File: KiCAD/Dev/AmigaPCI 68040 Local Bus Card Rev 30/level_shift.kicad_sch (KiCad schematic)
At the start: 26 parts, among them U101 74LVC245, U102 74LVC245, U103 74LVC245, U104 74LVC245, U105 74LVC245, U106 74LVC245, U107 74LVC245, U108 74LVC245, U109 SN74LVC16T245DLR, U110 SN74LVC16T245DLR

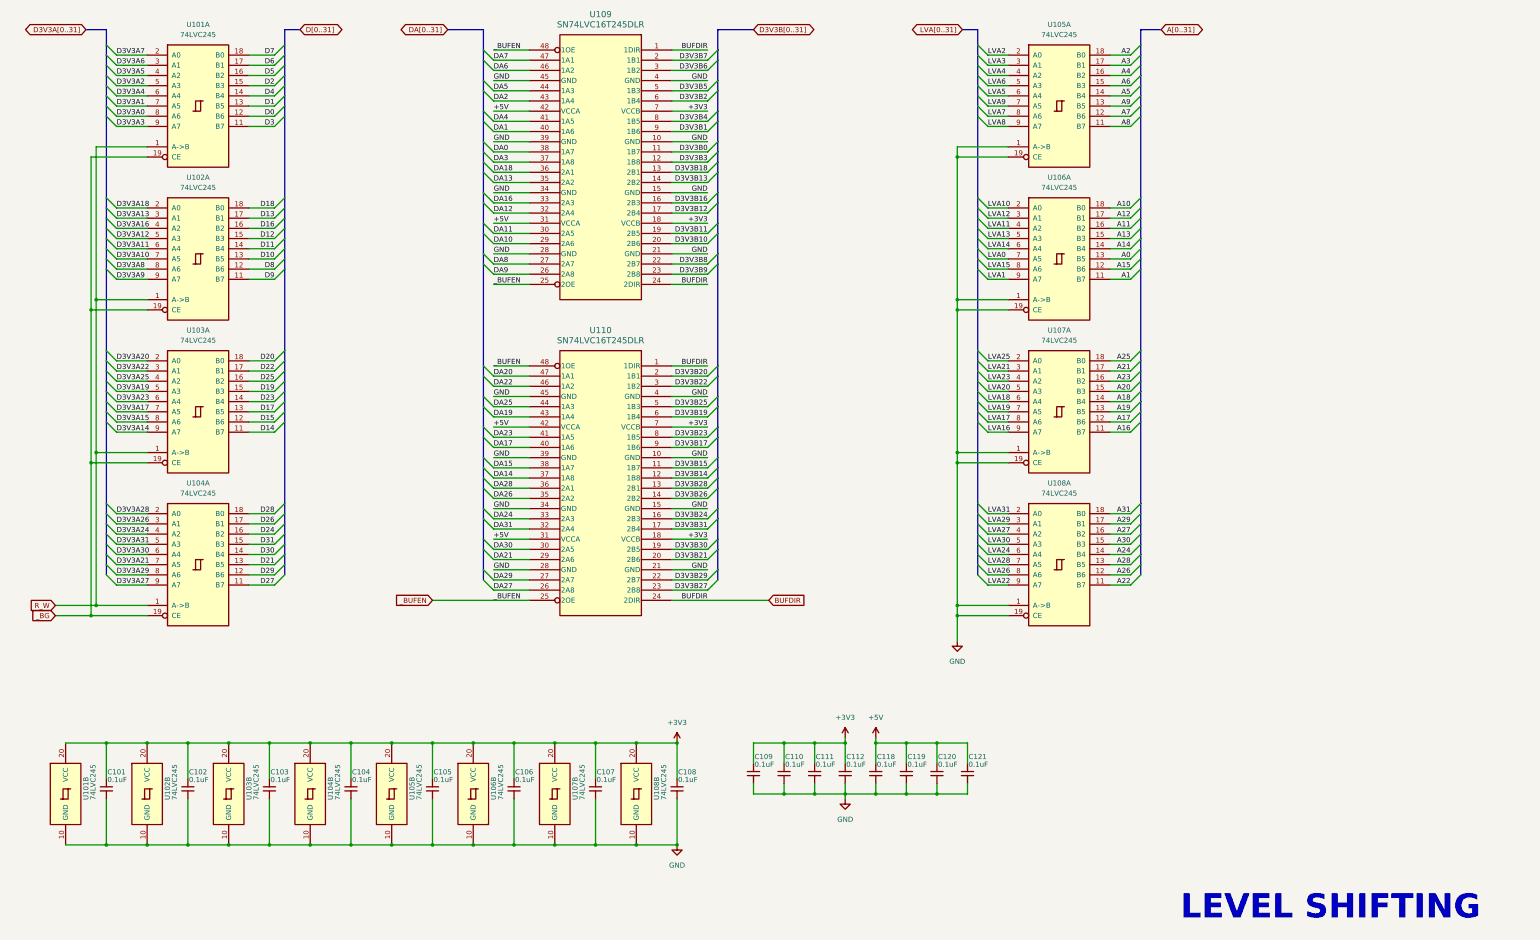
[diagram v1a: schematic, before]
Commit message: PCB Routing CPU Card 10-JUL-2024
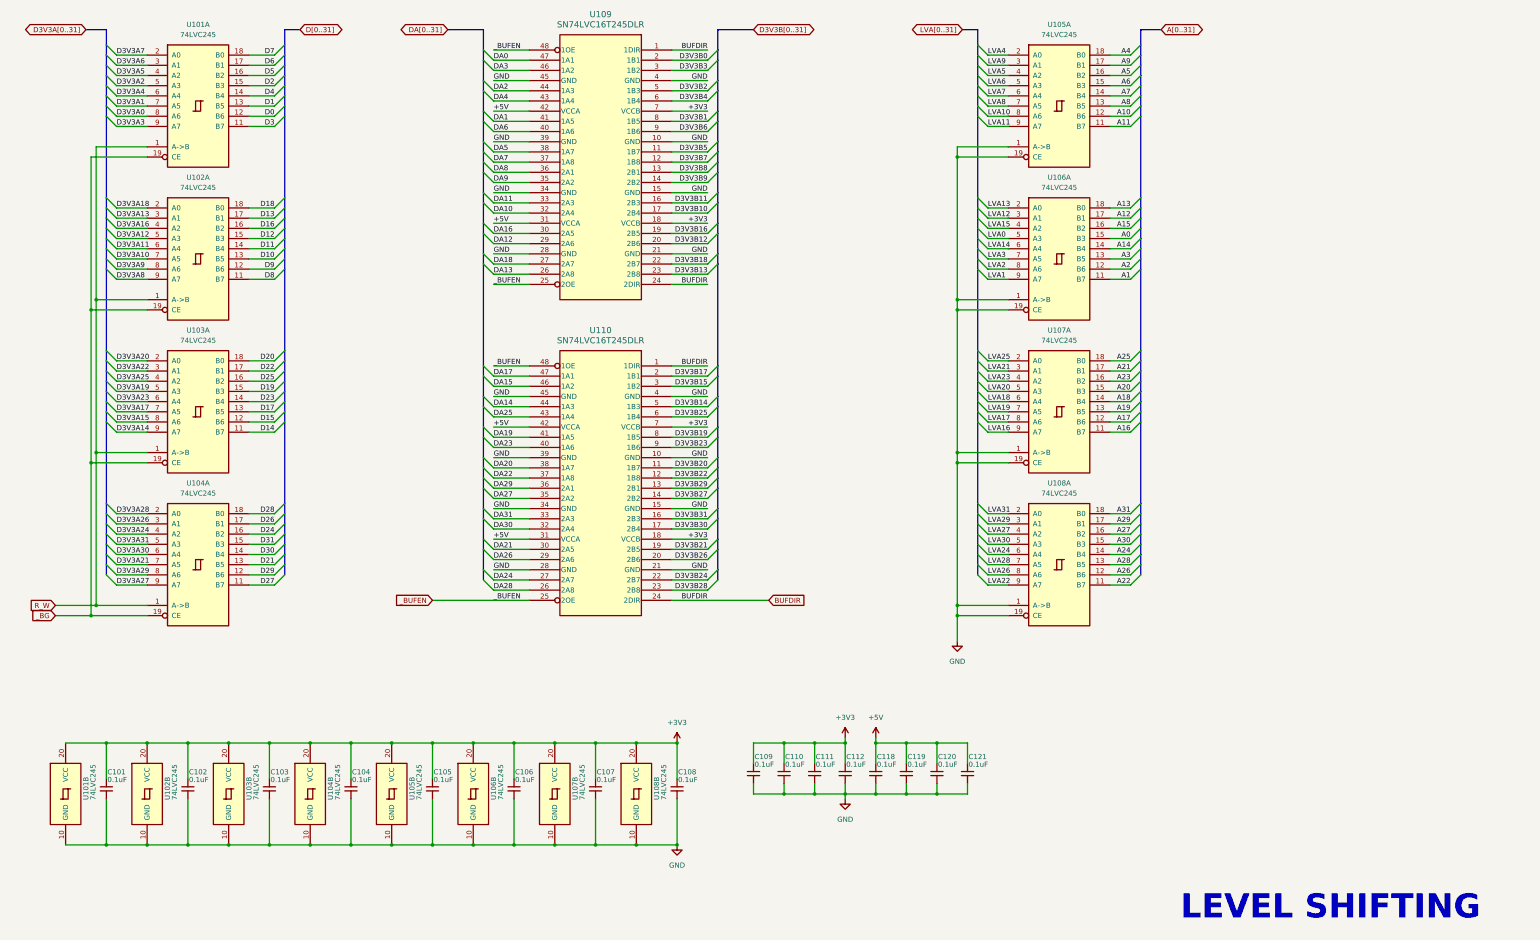
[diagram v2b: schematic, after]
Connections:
- net A0: now also U106.15 (B3); no longer U106.13 (B5)
- net A10: now also U105.12 (B6); no longer U106.18 (B0)
- net A11: now also U105.11 (B7); no longer U106.16 (B2)
- net A13: now also U106.18 (B0); no longer U106.15 (B3)
- net A15: now also U106.16 (B2); no longer U106.12 (B6)
- net A2: now also U106.12 (B6); no longer U105.18 (B0)
- net A3: now also U106.13 (B5); no longer U105.17 (B1)
- net A4: now also U105.18 (B0); no longer U105.16 (B2)
- net A5: now also U105.16 (B2); no longer U105.14 (B4)
- net A7: now also U105.14 (B4); no longer U105.12 (B6)
- net A8: now also U105.13 (B5); no longer U105.11 (B7)
- net A9: now also U105.17 (B1); no longer U105.13 (B5)
- net D3V3A8: now also U102.9 (A7); no longer U102.8 (A6)
- net D3V3A9: now also U102.8 (A6); no longer U102.9 (A7)
- net D3V3B0: now also U109.2 (1B1); no longer U109.11 (1B7)
- net D3V3B1: now also U109.8 (1B5); no longer U109.9 (1B6)
- net D3V3B10: now also U109.17 (2B4); no longer U109.20 (2B6)
- net D3V3B11: now also U109.16 (2B3); no longer U109.19 (2B5)
- net D3V3B12: now also U109.20 (2B6); no longer U109.17 (2B4)
- net D3V3B13: now also U109.23 (2B8); no longer U109.14 (2B2)
- net D3V3B14: now also U110.5 (1B3); no longer U110.12 (1B8)
- net D3V3B15: now also U110.3 (1B2); no longer U110.11 (1B7)
- net D3V3B16: now also U109.19 (2B5); no longer U109.16 (2B3)
- net D3V3B17: now also U110.2 (1B1); no longer U110.9 (1B6)
- net D3V3B18: now also U109.22 (2B7); no longer U109.13 (2B1)
- net D3V3B19: now also U110.8 (1B5); no longer U110.6 (1B4)
- net D3V3B2: now also U109.5 (1B3); no longer U109.6 (1B4)
- net D3V3B20: now also U110.11 (1B7); no longer U110.2 (1B1)
- net D3V3B21: now also U110.19 (2B5); no longer U110.20 (2B6)
- net D3V3B22: now also U110.12 (1B8); no longer U110.3 (1B2)
- net D3V3B23: now also U110.9 (1B6); no longer U110.8 (1B5)
- net D3V3B24: now also U110.22 (2B7); no longer U110.16 (2B3)
- net D3V3B25: now also U110.6 (1B4); no longer U110.5 (1B3)
- net D3V3B26: now also U110.20 (2B6); no longer U110.14 (2B2)
- net D3V3B27: now also U110.14 (2B2); no longer U110.23 (2B8)
- net D3V3B28: now also U110.23 (2B8); no longer U110.13 (2B1)
- net D3V3B29: now also U110.13 (2B1); no longer U110.22 (2B7)
- net D3V3B3: now also U109.3 (1B2); no longer U109.12 (1B8)
- net D3V3B30: now also U110.17 (2B4); no longer U110.19 (2B5)
- net D3V3B31: now also U110.16 (2B3); no longer U110.17 (2B4)
- net D3V3B4: now also U109.6 (1B4); no longer U109.8 (1B5)
- net D3V3B5: now also U109.11 (1B7); no longer U109.5 (1B3)
- net D3V3B6: now also U109.9 (1B6); no longer U109.3 (1B2)
- net D3V3B7: now also U109.12 (1B8); no longer U109.2 (1B1)
- net D3V3B8: now also U109.13 (2B1); no longer U109.22 (2B7)
- net D3V3B9: now also U109.14 (2B2); no longer U109.23 (2B8)
- net D8: now also U102.11 (B7); no longer U102.12 (B6)
- net D9: now also U102.12 (B6); no longer U102.11 (B7)
- net DA0: now also U109.47 (1A1); no longer U109.38 (1A7)
- net DA1: now also U109.41 (1A5); no longer U109.40 (1A6)
- net DA10: now also U109.32 (2A4); no longer U109.29 (2A6)
- net DA11: now also U109.33 (2A3); no longer U109.30 (2A5)
- net DA12: now also U109.29 (2A6); no longer U109.32 (2A4)
- net DA13: now also U109.26 (2A8); no longer U109.35 (2A2)
- net DA14: now also U110.44 (1A3); no longer U110.37 (1A8)
- net DA15: now also U110.46 (1A2); no longer U110.38 (1A7)
- net DA16: now also U109.30 (2A5); no longer U109.33 (2A3)
- net DA17: now also U110.47 (1A1); no longer U110.40 (1A6)
- net DA18: now also U109.27 (2A7); no longer U109.36 (2A1)
- net DA19: now also U110.41 (1A5); no longer U110.43 (1A4)
- net DA2: now also U109.44 (1A3); no longer U109.43 (1A4)
- net DA20: now also U110.38 (1A7); no longer U110.47 (1A1)
- net DA21: now also U110.30 (2A5); no longer U110.29 (2A6)
- net DA22: now also U110.37 (1A8); no longer U110.46 (1A2)
- net DA23: now also U110.40 (1A6); no longer U110.41 (1A5)
- net DA24: now also U110.27 (2A7); no longer U110.33 (2A3)
- net DA25: now also U110.43 (1A4); no longer U110.44 (1A3)
- net DA26: now also U110.29 (2A6); no longer U110.35 (2A2)
- net DA27: now also U110.35 (2A2); no longer U110.26 (2A8)
- net DA28: now also U110.26 (2A8); no longer U110.36 (2A1)
- net DA29: now also U110.36 (2A1); no longer U110.27 (2A7)
- net DA3: now also U109.46 (1A2); no longer U109.37 (1A8)
- net DA30: now also U110.32 (2A4); no longer U110.30 (2A5)
- net DA31: now also U110.33 (2A3); no longer U110.32 (2A4)
- net DA4: now also U109.43 (1A4); no longer U109.41 (1A5)
- net DA5: now also U109.38 (1A7); no longer U109.44 (1A3)
- net DA6: now also U109.40 (1A6); no longer U109.46 (1A2)
- net DA7: now also U109.37 (1A8); no longer U109.47 (1A1)
- net DA8: now also U109.36 (2A1); no longer U109.27 (2A7)
- net DA9: now also U109.35 (2A2); no longer U109.26 (2A8)
- net LVA0: now also U106.5 (A3); no longer U106.7 (A5)
- net LVA10: now also U105.8 (A6); no longer U106.2 (A0)
- net LVA11: now also U105.9 (A7); no longer U106.4 (A2)
- net LVA13: now also U106.2 (A0); no longer U106.5 (A3)
- net LVA15: now also U106.4 (A2); no longer U106.8 (A6)
- net LVA2: now also U106.8 (A6); no longer U105.2 (A0)
- net LVA3: now also U106.7 (A5); no longer U105.3 (A1)
- net LVA4: now also U105.2 (A0); no longer U105.4 (A2)
- net LVA5: now also U105.4 (A2); no longer U105.6 (A4)
- net LVA7: now also U105.6 (A4); no longer U105.8 (A6)
- net LVA8: now also U105.7 (A5); no longer U105.9 (A7)
- net LVA9: now also U105.3 (A1); no longer U105.7 (A5)

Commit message: CPU Local Bus Card Rev 3.0 Routing 15-JUL-2024
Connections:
- net A16: now also U108.11 (B7); no longer U107.11 (B7)
- net A17: now also U108.12 (B6); no longer U107.12 (B6)
- net A18: now also U108.14 (B4); no longer U107.14 (B4)
- net A19: now also U108.13 (B5); no longer U107.13 (B5)
- net A20: now also U108.15 (B3); no longer U107.15 (B3)
- net A21: now also U108.16 (B2); no longer U107.17 (B1)
- net A22: now also U107.13 (B5); no longer U108.11 (B7)
- net A23: now also U107.18 (B0); no longer U107.16 (B2)
- net A24: now also U108.17 (B1); no longer U108.14 (B4)
- net A25: now also U107.17 (B1); no longer U107.18 (B0)
- net A26: now also U107.14 (B4); no longer U108.12 (B6)
- net A27: now also U108.18 (B0); no longer U108.16 (B2)
- net A28: now also U107.15 (B3); no longer U108.13 (B5)
- net A29: now also U107.11 (B7); no longer U108.17 (B1)
- net A30: now also U107.16 (B2); no longer U108.15 (B3)
- net A31: now also U107.12 (B6); no longer U108.18 (B0)
- net LVA16: now also U108.9 (A7); no longer U107.9 (A7)
- net LVA17: now also U108.8 (A6); no longer U107.8 (A6)
- net LVA18: now also U108.6 (A4); no longer U107.6 (A4)
- net LVA19: now also U108.7 (A5); no longer U107.7 (A5)
- net LVA20: now also U108.5 (A3); no longer U107.5 (A3)
- net LVA21: now also U108.4 (A2); no longer U107.3 (A1)
- net LVA22: now also U107.7 (A5); no longer U108.9 (A7)
- net LVA23: now also U107.2 (A0); no longer U107.4 (A2)
- net LVA24: now also U108.3 (A1); no longer U108.6 (A4)
- net LVA25: now also U107.3 (A1); no longer U107.2 (A0)
- net LVA26: now also U107.6 (A4); no longer U108.8 (A6)
- net LVA27: now also U108.2 (A0); no longer U108.4 (A2)
- net LVA28: now also U107.5 (A3); no longer U108.7 (A5)
- net LVA29: now also U107.9 (A7); no longer U108.3 (A1)
- net LVA30: now also U107.4 (A2); no longer U108.5 (A3)
- net LVA31: now also U107.8 (A6); no longer U108.2 (A0)
- net R_W renamed R_W-3V

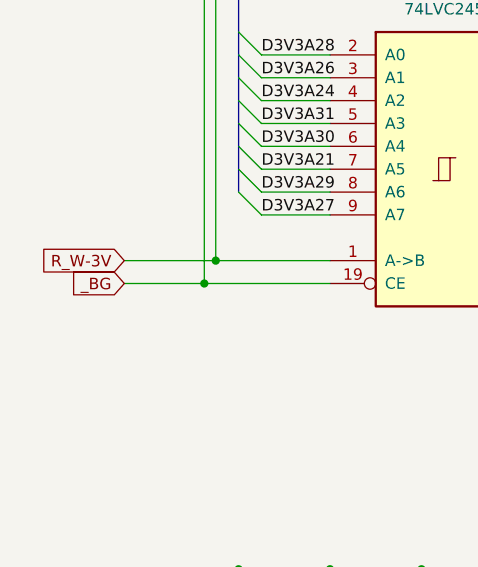
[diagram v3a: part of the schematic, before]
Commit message: CPU Local Bus Card routing. 15-JUL-2024
Board is now 6 layers to provide adequate +5V to the 68040.
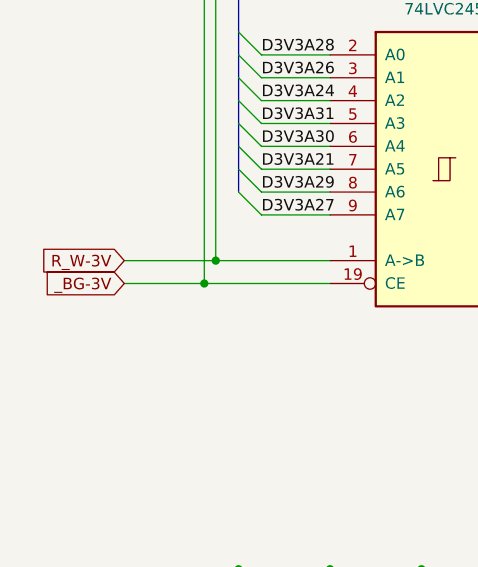
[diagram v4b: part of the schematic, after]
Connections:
- net _BG renamed _BG-3V
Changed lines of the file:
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@@
 	(title_block
 		(title "AmigaPCI 68040")
-		(date "2024-07-14")
+		(date "2024-07-15")
 		(rev "3.0")
 	)
@@
 		)
 	)
-	(global_label "_BG"
+	(global_label "_BG-3V"
 		(shape input)
 		(at 33.02 170.18 180)
@@
 		)
 		(property "Intersheetrefs" "${INTERSHEET_REFS}"
-			(at 26.797 170.18 0)
+			(at 23.368 170.18 0)
 			(effects
 				(font

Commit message: CPU Local Bus Card Rev 3.0 Routing 18-JUL-2024
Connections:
- net _BG-3V renamed _BGA
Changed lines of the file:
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@@
 	(title_block
 		(title "AmigaPCI 68040")
-		(date "2024-07-15")
+		(date "2024-07-18")
 		(rev "3.0")
 	)
@@
 		)
 	)
-	(global_label "_BG-3V"
+	(global_label "_BGA"
 		(shape input)
 		(at 33.02 170.18 180)

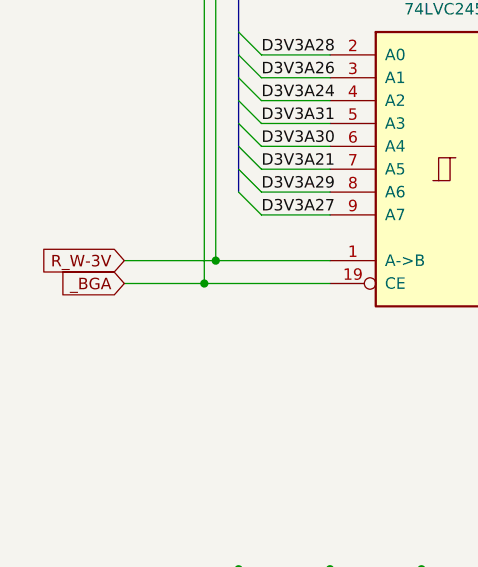
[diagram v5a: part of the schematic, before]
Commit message: CPU Local Bus Card schematics and routing, misc changes to readme's.
This should be project lock for the Rev 3.0 CPU Local Bus Card.
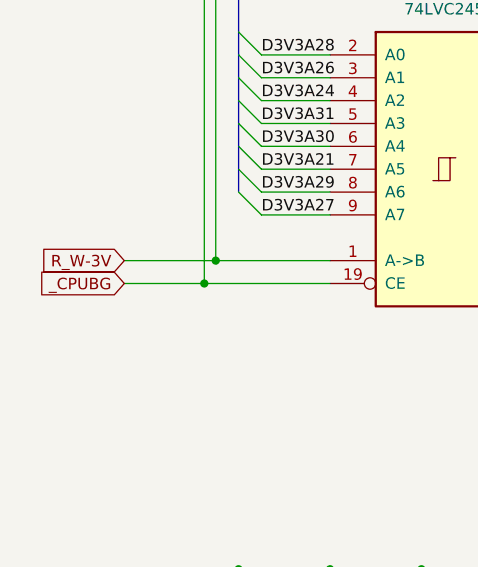
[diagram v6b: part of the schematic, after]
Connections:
- net _BGA renamed _CPUBG
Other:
- title: AmigaPCI 68040 -> AmigaPCI 68040 Local Bus Card
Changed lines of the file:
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@@
 	(paper "USLedger")
 	(title_block
-		(title "AmigaPCI 68040")
-		(date "2024-07-18")
+		(title "AmigaPCI 68040 Local Bus Card")
+		(date "2024-07-20")
 		(rev "3.0")
 	)
@@
 		)
 	)
-	(global_label "_BGA"
+	(global_label "_CPUBG"
 		(shape input)
 		(at 33.02 170.18 180)
